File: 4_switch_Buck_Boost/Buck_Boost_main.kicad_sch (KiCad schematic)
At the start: 95 parts, among them J1 Conn_02x02_Counter_Clockwise, J2 Screw_Terminal_2x5.08, J3 Screw_Terminal_2x2.54, J4 Screw_Terminal_2x5.08, Q101 2N7002K, Q102 NVMFS6H836NLT1G, Q103 BSS83P, Q104 BSC070N10LS5, Q105 BSC070N10LS5, Q106 BSC070N10LS5, Q107 BSC070N10LS5, U1 LT8390EUFD_PBF, U101 LTC4372CMS8-PBF

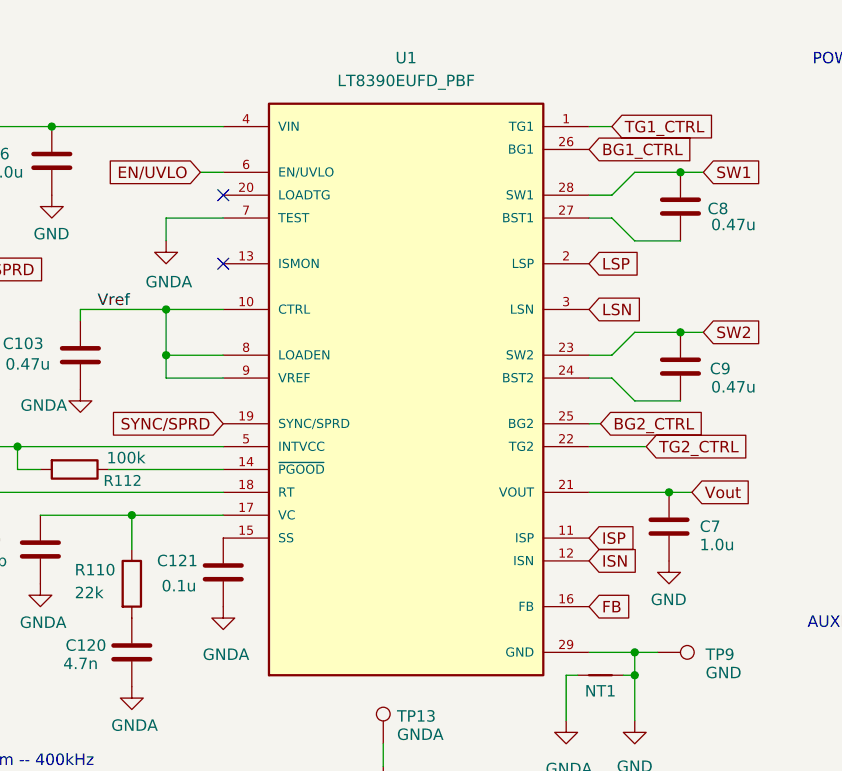
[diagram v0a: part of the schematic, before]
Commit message: Add LT8390EFE#PBF footprint
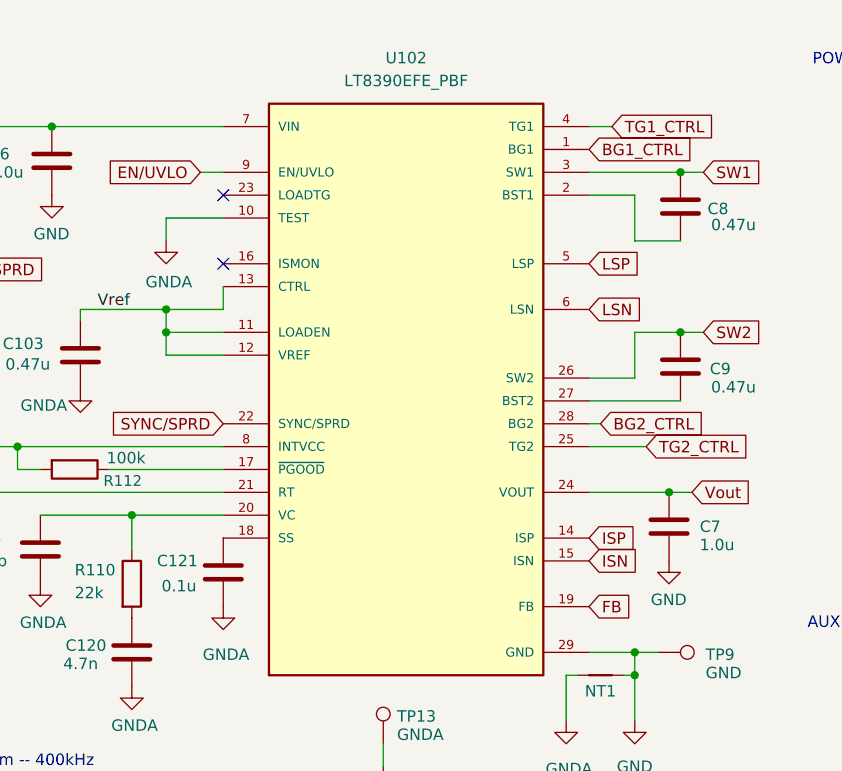
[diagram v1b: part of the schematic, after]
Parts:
- removed U1: LT8390EUFD_PBF, LT:QFN50P500X400X80-29N, symbol LT:LT8390EUFD_PBF
- added U102: LT8390EFE_PBF, LT:05-08-1663_ADI, symbol LT8390EFE_PBF:LT8390EFE_PBF
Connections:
- net BG1_CTRL: now also U102.1 (BG1)
- net BG2_CTRL: now also U102.28 (BG2)
- net EN/UVLO: now also U102.9 (EN/UVLO)
- net FB: now also U102.19 (FB)
- net GND: now also U102.29 (GND)
- net GNDA: now also U102.10 (TEST)
- net INTVCC: now also U102.8 (INTVCC)
- net ISN: now also U102.15 (ISN)
- net ISP: now also U102.14 (ISP)
- net LSN: now also U102.6 (LSN)
- net LSP: now also U102.5 (LSP)
- net SW1: now also U102.3 (SW1)
- net SW2: now also U102.26 (SW2)
- net SYNC/SPRD: now also U102.22 (SYNC/SPRD)
- net TG1_CTRL: now also U102.4 (TG1)
- net TG2_CTRL: now also U102.25 (TG2)
- net Vin: now also U102.7 (VIN)
- net Vout: now also U102.24 (VOUT)
- net Vref: now also U102.11 (LOADEN), U102.12 (VREF), U102.13 (CTRL)
- net at C119.1, R110.1: now also U102.20 (VC)
- net at C9.1: now also U102.27 (BST2)
- net at C121.1: now also U102.18 (SS)
- net at C8.1: now also U102.2 (BST1)
- net at R112.1: now also U102.17 (~{PGOOD})
- net at R111.2, TP5.1: now also U102.21 (RT)

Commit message: Adding DPN - not done yet
clean stuff and some dpn

cleanup AND moar dpn

more cleanup
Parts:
- C1, C101, C106, C112, C113: DPN (none) -> 445-5972-2-ND; now left out of the parts list
- C102, C114, C115, C116, C118, C121, C129, C132, C5: DPN (none) -> 490-3285-1-ND
- C103, C8, C9: DPN (none) -> 490-11994-1-ND
- C104: value 100n -> 0.1u; DPN (none) -> 490-3285-1-ND
- C107, C108, C117: DPN (none) -> 732-875585853004CT-ND
- C109, C110, C111: DPN (none) -> 732-875575853003CT-ND
- C119: DPN (none) -> 490-1427-1-ND
- C120: DPN (none) -> 490-9669-1-ND
- C123, C124: DPN (none) -> 490-1443-1-ND
- C131, C4: DPN (none) -> 490-17777-1-ND
- C6, C7: DPN (none) -> 490-12330-1-ND
- J1: footprint Connector_PinHeader_1.00mm:PinHeader_2x02_P1.00mm_Vertical -> Connector_PinHeader_2.54mm:PinHeader_2x02_P2.54mm_Vertical; DPN (none) -> 612-TSW-102-07-G-D-ND
- Q102: DPN (none) -> 488-NVMFS6H836NLT1GCT-ND
- Q103: DPN (none) -> BSS83PH6327XTSA1CT-ND
- Q104, Q105, Q106, Q107: DPN (none) -> 448-BSC070N10LS5ATMA1CT-ND
- R1, R2, R3: DPN (none) -> RMCF0603FT4K70CT-ND
- R10, R103, R104: DPN (none) -> 13-RT0603BRD0750KLCT-ND
- R105, R106, R107, R109: value 100K -> 100k; DPN (none) -> RMCF0603FT100KCT-ND
- R110: DPN (none) -> RMCF0603FT22K0CT-ND
- R111: DPN (none) -> RMCF0603FT56K0CT-ND
- R112: DPN (none) -> RMCF0603FT100KCT-ND
- R113, R114: footprint Capacitor_SMD:C_0805_2012Metric -> rsx_resistors:R_0603_1608Metric; DPN (none) -> RMCF0603FT4R70CT-ND
- R115, R116, R117, R118: DPN (none) -> RMCF0603FT4R70CT-ND
- R7, R8: DPN (none) -> 408-KRL3216T4-M-R003-F-T1CT-ND
- R9: DPN (none) -> RMCF0603FT300KCT-ND
- TP1, TP10, TP11, TP12, TP13, TP2, TP5, TP6, TP7, TP8, TP9: now left out of the parts list
- TP3, TP4: footprint TestPoint:TestPoint_Loop_D1.80mm_Drill1.0mm_Beaded -> TestPoint:TestPoint_Loop_D2.50mm_Drill1.0mm_LowProfile; DPN (none) -> 36-5001-ND; now left out of the parts list
- U101: DPN (none) -> 505-LTC4372CMS8#PBF-ND
- U102: DPN (none) -> 505-LT8390EFE#PBF-ND

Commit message: finish analog connections change rsense footprint
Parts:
- R7: footprint Littelfuse_L4CA0612_KiCad9:Littelfuse_L4CA0612_4Terminal -> WLTM:WLTM0612_R002-R100_Kelvin
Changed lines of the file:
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@@
 			)
 		)
-		(property "Footprint" "Littelfuse_L4CA0612_KiCad9:Littelfuse_L4CA0612_4Terminal"
+		(property "Footprint" "WLTM:WLTM0612_R002-R100_Kelvin"
 			(at 231.14 41.91 0)
 			(effects
